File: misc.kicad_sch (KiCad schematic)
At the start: 22 parts, among them J7 Conn_ARM_JTAG_SWD_10, SW2 SW_DIP_x02, U1 MIMX8MM6DVTLZAA, Y3 24Mhz

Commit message: change USB-UART conn, add new 0402 fp, more pcb work
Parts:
- C141, C142: footprint Capacitor_SMD:C_0402_1005Metric -> qsbc:C_0402_1005Metric
- R88, R89, R90, R91, R92, R93, R94, R95, R96, R97, R98, R99: footprint Resistor_SMD:R_0402_1005Metric -> qsbc:R_0402_1005Metric
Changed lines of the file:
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@@
       (effects (font (size 1.27 1.27)) (justify left))
     )
-    (property "Footprint" "Capacitor_SMD:C_0402_1005Metric" (id 2) (at 98.7552 135.89 0)
+    (property "Footprint" "qsbc:C_0402_1005Metric" (id 2) (at 98.7552 135.89 0)
       (effects (font (size 1.27 1.27)) hide)
     )
@@
       (effects (font (size 1.27 1.27)) (justify left))
     )
-    (property "Footprint" "Resistor_SMD:R_0402_1005Metric" (id 2) (at 223.012 104.14 90)
+    (property "Footprint" "qsbc:R_0402_1005Metric" (id 2) (at 223.012 104.14 90)
       (effects (font (size 1.27 1.27)) hide)
     )
@@
       (effects (font (size 1.27 1.27)) (justify left))
     )
-    (property "Footprint" "Resistor_SMD:R_0402_1005Metric" (id 2) (at 212.852 35.56 90)
+    (property "Footprint" "qsbc:R_0402_1005Metric" (id 2) (at 212.852 35.56 90)
       (effects (font (size 1.27 1.27)) hide)
     )
@@
       (effects (font (size 1.27 1.27)) (justify left))
     )
-    (property "Footprint" "Resistor_SMD:R_0402_1005Metric" (id 2) (at 202.692 35.56 90)
+    (property "Footprint" "qsbc:R_0402_1005Metric" (id 2) (at 202.692 35.56 90)
       (effects (font (size 1.27 1.27)) hide)
     )
@@
       (effects (font (size 1.27 1.27)) (justify left))
     )
-    (property "Footprint" "Resistor_SMD:R_0402_1005Metric" (id 2) (at 94.742 58.42 90)
+    (property "Footprint" "qsbc:R_0402_1005Metric" (id 2) (at 94.742 58.42 90)
       (effects (font (size 1.27 1.27)) hide)
     )
@@
     (property "Reference" "R91" (id 0) (at 109.22 105.41 90))
     (property "Value" "510K" (id 1) (at 109.22 107.95 90))
-    (property "Footprint" "Resistor_SMD:R_0402_1005Metric" (id 2) (at 109.22 113.538 90)
+    (property "Footprint" "qsbc:R_0402_1005Metric" (id 2) (at 109.22 113.538 90)
       (effects (font (size 1.27 1.27)) hide)
     )
@@
       (effects (font (size 1.27 1.27)) (justify left))
     )
-    (property "Footprint" "Resistor_SMD:R_0402_1005Metric" (id 2) (at 233.172 104.14 90)
+    (property "Footprint" "qsbc:R_0402_1005Metric" (id 2) (at 233.172 104.14 90)
       (effects (font (size 1.27 1.27)) hide)
     )
@@
       (effects (font (size 1.27 1.27)) (justify left))
     )
-    (property "Footprint" "Resistor_SMD:R_0402_1005Metric" (id 2) (at 212.852 104.14 90)
+    (property "Footprint" "qsbc:R_0402_1005Metric" (id 2) (at 212.852 104.14 90)
       (effects (font (size 1.27 1.27)) hide)
     )
@@
       (effects (font (size 1.27 1.27)) (justify left))
     )
-    (property "Footprint" "Resistor_SMD:R_0402_1005Metric" (id 2) (at 115.062 58.42 90)
+    (property "Footprint" "qsbc:R_0402_1005Metric" (id 2) (at 115.062 58.42 90)
       (effects (font (size 1.27 1.27)) hide)
     )
@@
       (effects (font (size 1.27 1.27)) (justify left))
     )
-    (property "Footprint" "Resistor_SMD:R_0402_1005Metric" (id 2) (at 202.692 104.14 90)
+    (property "Footprint" "qsbc:R_0402_1005Metric" (id 2) (at 202.692 104.14 90)
       (effects (font (size 1.27 1.27)) hide)
     )
@@
       (effects (font (size 1.27 1.27)) (justify left))
     )
-    (property "Footprint" "Capacitor_SMD:C_0402_1005Metric" (id 2) (at 121.6152 135.89 0)
+    (property "Footprint" "qsbc:C_0402_1005Metric" (id 2) (at 121.6152 135.89 0)
       (effects (font (size 1.27 1.27)) hide)
     )
@@
       (effects (font (size 1.27 1.27)) (justify left))
     )
-    (property "Footprint" "Resistor_SMD:R_0402_1005Metric" (id 2) (at 243.332 81.28 90)
+    (property "Footprint" "qsbc:R_0402_1005Metric" (id 2) (at 243.332 81.28 90)
       (effects (font (size 1.27 1.27)) hide)
     )
@@
       (effects (font (size 1.27 1.27)) (justify left))
     )
-    (property "Footprint" "Resistor_SMD:R_0402_1005Metric" (id 2) (at 104.902 58.42 90)
+    (property "Footprint" "qsbc:R_0402_1005Metric" (id 2) (at 104.902 58.42 90)
       (effects (font (size 1.27 1.27)) hide)
     )
@@
     (property "Reference" "R90" (id 0) (at 107.95 85.09 90))
     (property "Value" "0R" (id 1) (at 107.95 87.63 90))
-    (property "Footprint" "Resistor_SMD:R_0402_1005Metric" (id 2) (at 107.95 93.218 90)
-      (effects (font (size 1.27 1.27)) hide)
-    )
+    (property "Footprint" "qsbc:R_0402_1005Metric" (id 2) (at 107.95 93.218 90)
+      (effects (font (size 1.27 1.27)) hide)
+    )

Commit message: swap usb ctrl signals for layout
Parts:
- TP22, TP23, TP24, TP25: footprint TestPoint:TestPoint_Pad_D1.0mm -> qsbc:TestPoint_Pad_D0.4mm
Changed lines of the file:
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@@
       (effects (font (size 1.27 1.27)) (justify left))
     )
-    (property "Footprint" "TestPoint:TestPoint_Pad_D1.0mm" (id 2) (at 86.36 64.77 0)
+    (property "Footprint" "qsbc:TestPoint_Pad_D0.4mm" (id 2) (at 86.36 64.77 0)
       (effects (font (size 1.27 1.27)) hide)
     )
@@
       (effects (font (size 1.27 1.27)) (justify left))
     )
-    (property "Footprint" "TestPoint:TestPoint_Pad_D1.0mm" (id 2) (at 73.66 64.77 0)
+    (property "Footprint" "qsbc:TestPoint_Pad_D0.4mm" (id 2) (at 73.66 64.77 0)
       (effects (font (size 1.27 1.27)) hide)
     )
@@
       (effects (font (size 1.27 1.27)) (justify left))
     )
-    (property "Footprint" "TestPoint:TestPoint_Pad_D1.0mm" (id 2) (at 48.26 64.77 0)
+    (property "Footprint" "qsbc:TestPoint_Pad_D0.4mm" (id 2) (at 48.26 64.77 0)
       (effects (font (size 1.27 1.27)) hide)
     )
@@
       (effects (font (size 1.27 1.27)) (justify left))
     )
-    (property "Footprint" "TestPoint:TestPoint_Pad_D1.0mm" (id 2) (at 60.96 64.77 0)
-      (effects (font (size 1.27 1.27)) hide)
-    )
+    (property "Footprint" "qsbc:TestPoint_Pad_D0.4mm" (id 2) (at 60.96 64.77 0)
+      (effects (font (size 1.27 1.27)) hide)
+    )

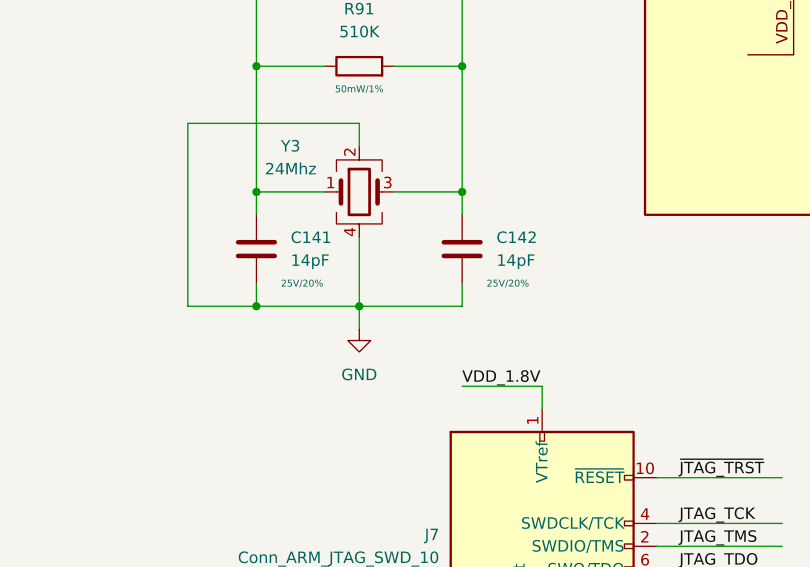
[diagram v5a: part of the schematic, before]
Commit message: bom work, change uart level shifter and m.2 socket
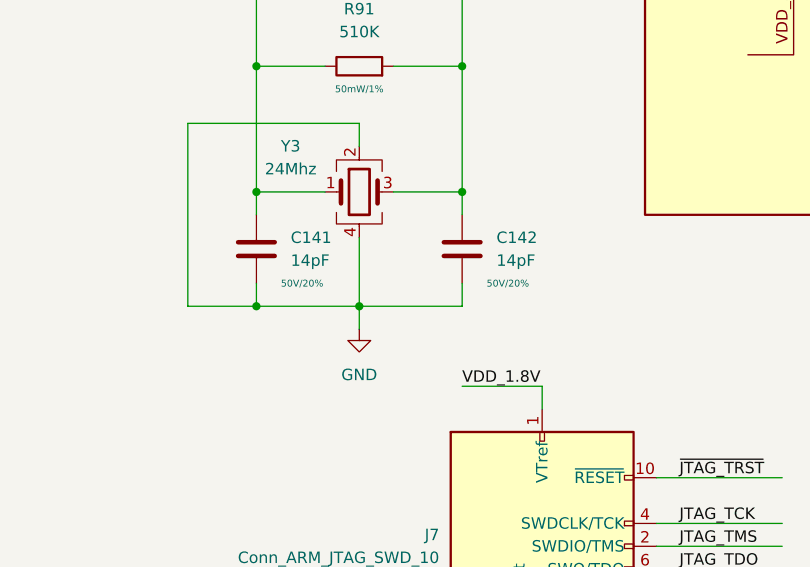
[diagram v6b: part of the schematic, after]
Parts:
- C141, C142: MPN (none) -> 04025U140FAT2A; Rating 25V/20% -> 50V/20%
- J7: MPN (none) -> FTSH-105-01-F-D-007-K
- R88, R89, R92, R94, R98: MPN (none) -> RC0402FR-07100KL
- R90: MPN (none) -> RC0402FR-070RL
- R91: MPN (none) -> RC0402FR-07510KL
- R93, R95, R96, R97, R99: MPN (none) -> RC0402FR-0710KL
- SW2: MPN (none) -> DHN-02-V-T/R
- U1: MPN (none) -> MIMX8MM6DVTLZAA
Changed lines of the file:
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@@
       (effects (font (size 1.27 1.27)) hide)
     )
-    (property "Rating" "25V/20%" (id 4) (at 102.87 135.89 0)
-      (effects (font (size 0.762 0.762)))
+    (property "Rating" "50V/20%" (id 4) (at 102.87 135.89 0)
+      (effects (font (size 0.762 0.762)))
+    )
+    (property "MPN" "04025U140FAT2A" (id 5) (at 97.79 132.08 0)
+      (effects (font (size 1.27 1.27)) hide)
     )
     (pin "1")
@@
     (property "Rating" "50mW/1%" (id 4) (at 229.87 107.95 0)
       (effects (font (size 0.762 0.762)))
+    )
+    (property "MPN" "RC0402FR-0710KL" (id 5) (at 224.79 104.14 0)
+      (effects (font (size 1.27 1.27)) hide)
     )
     (pin "1")
@@
     (property "Datasheet" "https://www.nxp.com/docs/en/data-sheet/IMX8MMCEC.pdf" (id 3) (at 162.56 265.43 0)
       (effects (font (size 1.27 1.27)) (justify left bottom) hide)
+    )
+    (property "MPN" "MIMX8MM6DVTLZAA" (id 4) (at 161.29 71.12 0)
+      (effects (font (size 1.27 1.27)) hide)
     )
     (pin "A24")
@@
       (effects (font (size 0.762 0.762)))
     )
+    (property "MPN" "RC0402FR-0710KL" (id 5) (at 214.63 35.56 0)
+      (effects (font (size 1.27 1.27)) hide)
+    )
     (pin "1")
     (pin "2")
@@
       (effects (font (size 0.762 0.762)))
     )
+    (property "MPN" "RC0402FR-0710KL" (id 5) (at 204.47 35.56 0)
+      (effects (font (size 1.27 1.27)) hide)
+    )
     (pin "1")
     (pin "2")
@@
     (property "Rating" "50mW/1%" (id 4) (at 101.6 62.23 0)
       (effects (font (size 0.762 0.762)))
+    )
+    (property "MPN" "RC0402FR-07100KL" (id 5) (at 96.52 58.42 0)
+      (effects (font (size 1.27 1.27)) hide)
     )
     (pin "1")
@@
       (effects (font (size 0.762 0.762)))
     )
+    (property "MPN" "RC0402FR-07510KL" (id 5) (at 109.22 111.76 0)
+      (effects (font (size 1.27 1.27)) hide)
+    )
     (pin "1")
     (pin "2")
@@
       (effects (font (size 0.762 0.762)))
     )
+    (property "MPN" "RC0402FR-07100KL" (id 5) (at 234.95 104.14 0)
+      (effects (font (size 1.27 1.27)) hide)
+    )
     (pin "1")
     (pin "2")
@@
       (effects (font (size 0.762 0.762)))
     )
+    (property "MPN" "RC0402FR-0710KL" (id 5) (at 214.63 104.14 0)
+      (effects (font (size 1.27 1.27)) hide)
+    )
     (pin "1")
     (pin "2")
@@
     (property "Rating" "50mW/1%" (id 4) (at 121.92 62.23 0)
       (effects (font (size 0.762 0.762)))
+    )
+    (property "MPN" "RC0402FR-07100KL" (id 5) (at 116.84 58.42 0)
+      (effects (font (size 1.27 1.27)) hide)
     )
     (pin "1")
@@
       (effects (font (size 0.762 0.762)))
     )
+    (property "MPN" "RC0402FR-07100KL" (id 5) (at 204.47 104.14 0)
+      (effects (font (size 1.27 1.27)) hide)
+    )
     (pin "1")
     (pin "2")
@@
       (effects (font (size 1.27 1.27)) hide)
     )
-    (property "Rating" "25V/20%" (id 4) (at 125.73 135.89 0)
-      (effects (font (size 0.762 0.762)))
+    (property "Rating" "50V/20%" (id 4) (at 125.73 135.89 0)
+      (effects (font (size 0.762 0.762)))
+    )
+    (property "MPN" "04025U140FAT2A" (id 5) (at 120.65 132.08 0)
+      (effects (font (size 1.27 1.27)) hide)
     )
     (pin "1")
@@
       (effects (font (size 0.762 0.762)))
     )
+    (property "MPN" "RC0402FR-0710KL" (id 5) (at 245.11 81.28 0)
+      (effects (font (size 1.27 1.27)) hide)
+    )
     (pin "1")
     (pin "2")
@@
     (property "Rating" "50mW/1%" (id 4) (at 111.76 62.23 0)
       (effects (font (size 0.762 0.762)))
+    )
+    (property "MPN" "RC0402FR-07100KL" (id 5) (at 106.68 58.42 0)
+      (effects (font (size 1.27 1.27)) hide)
     )
     (pin "1")
@@
     )
     (property "Datasheet" "~" (id 3) (at 207.01 52.07 0)
+      (effects (font (size 1.27 1.27)) hide)
+    )
+    (property "MPN" "DHN-02-V-T/R" (id 4) (at 207.01 52.07 0)
       (effects (font (size 1.27 1.27)) hide)
     )
@@
       (effects (font (size 1.27 1.27)) hide)
     )
+    (property "MPN" "RC0402FR-070RL" (id 4) (at 107.95 91.44 0)
+      (effects (font (size 1.27 1.27)) hide)
+    )
     (pin "1")
     (pin "2")
@@
       (effects (font (size 1.27 1.27)) hide)
     )
+    (property "MPN" "FTSH-105-01-F-D-007-K" (id 4) (at 129.54 165.1 0)
+      (effects (font (size 1.27 1.27)) hide)
+    )

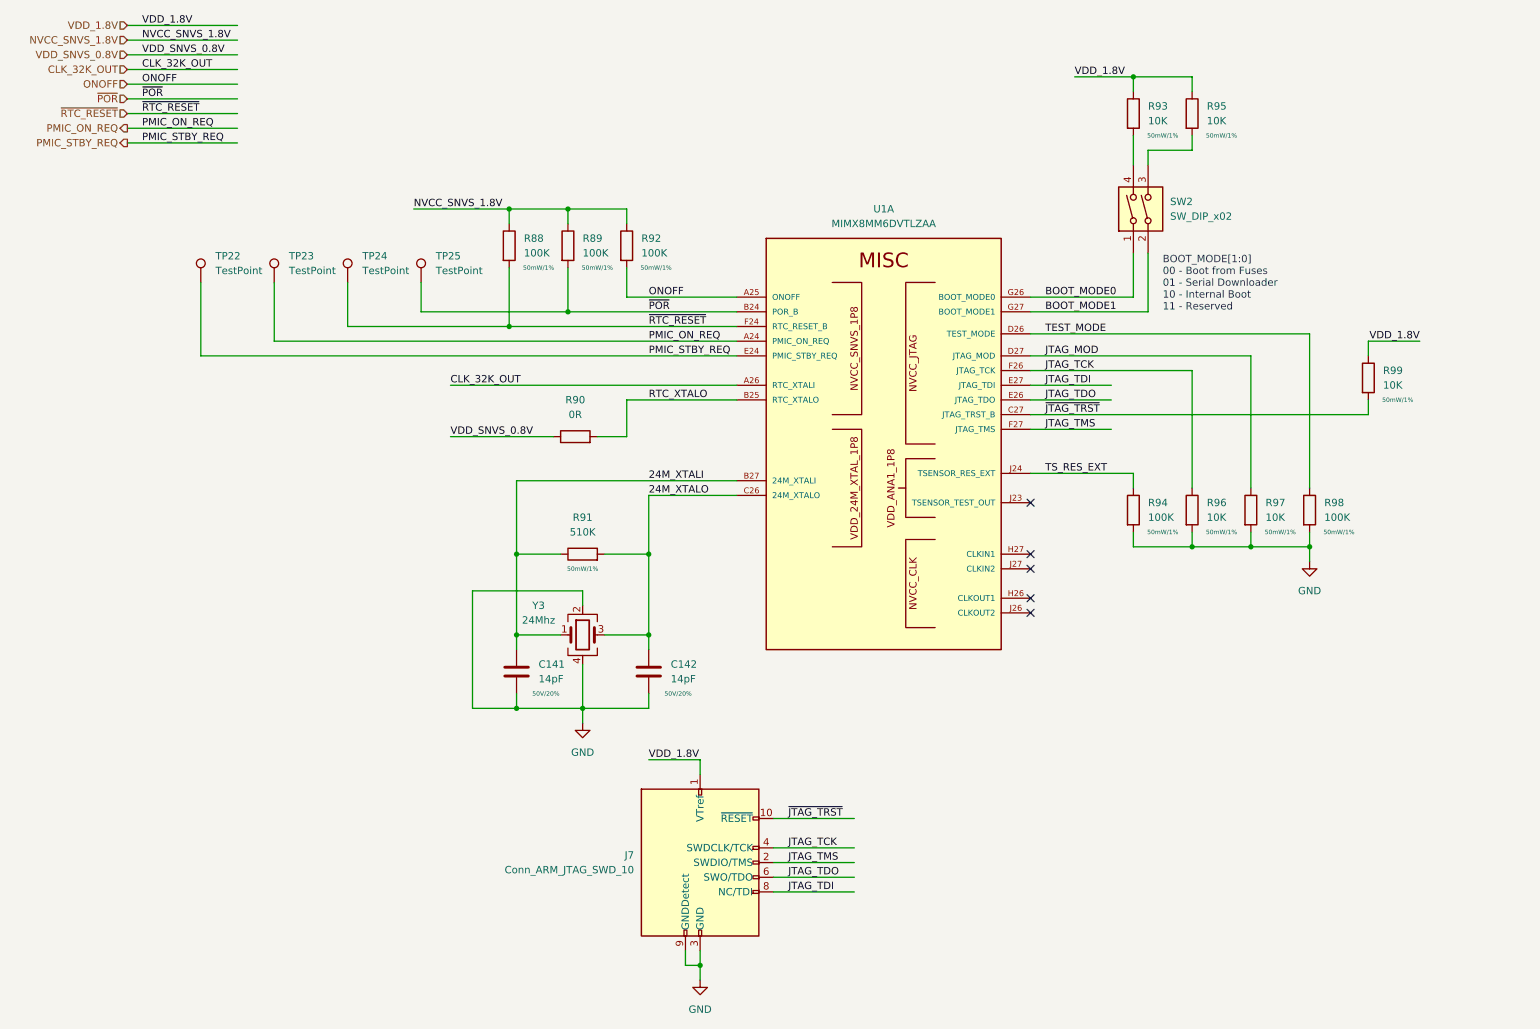
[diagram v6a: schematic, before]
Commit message: ddr length matching work, misc cleanup
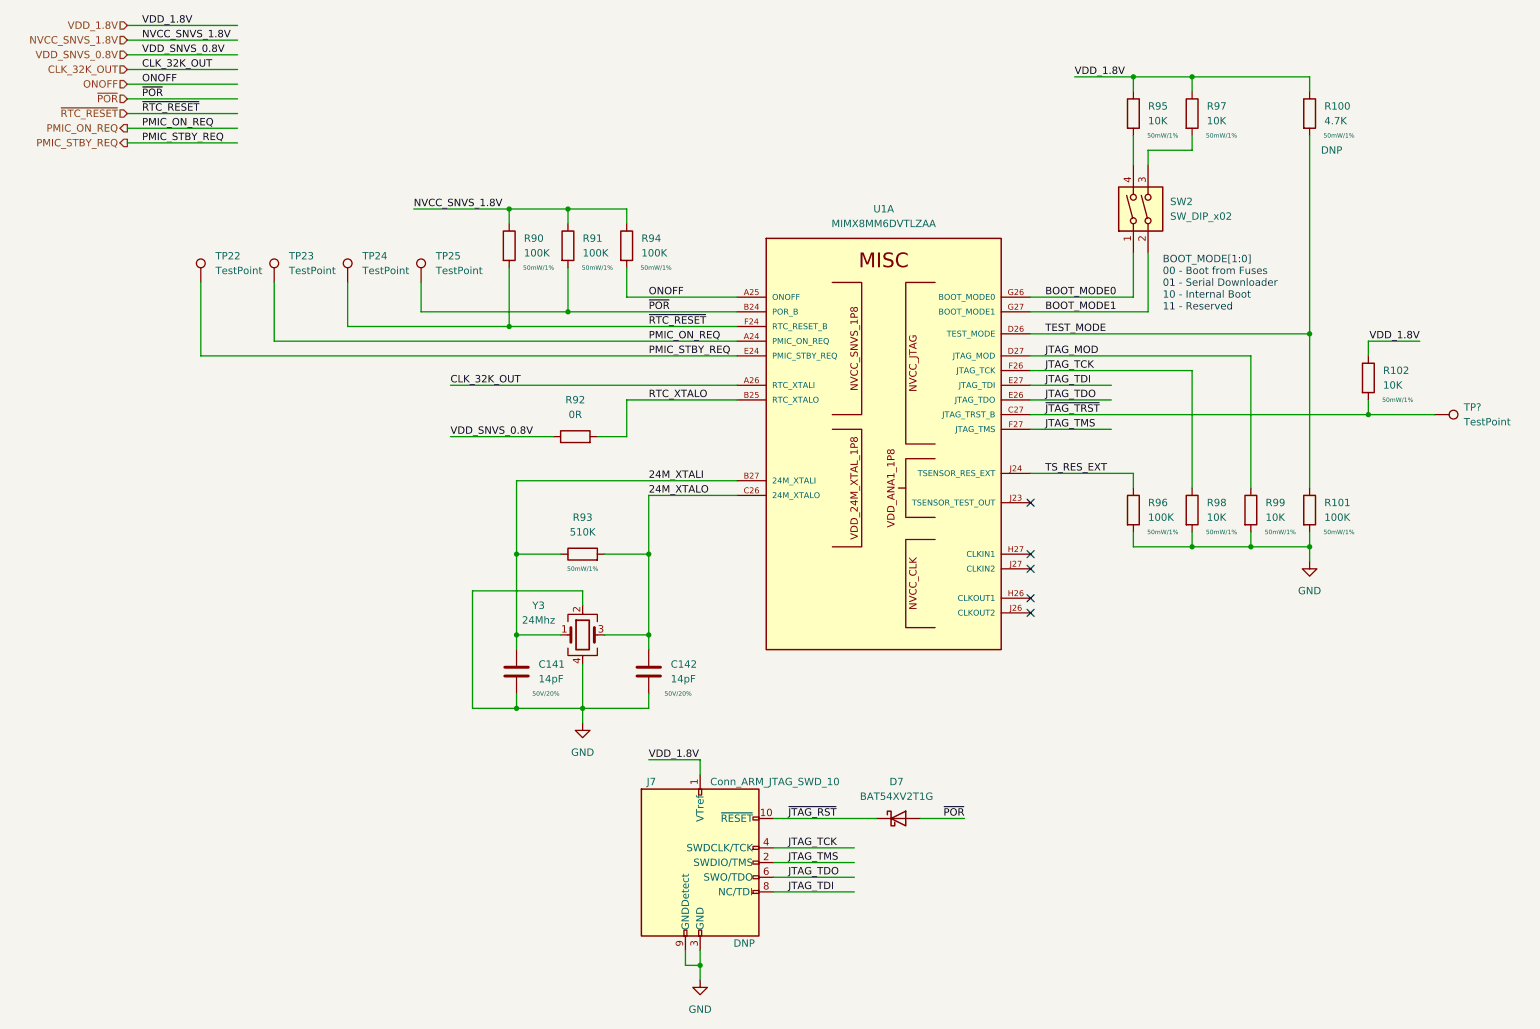
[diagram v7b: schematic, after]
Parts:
- added D7: BAT54XV2T1G, Diode_SMD:D_SOD-523, symbol Device:D_Schottky
- added R100: 4.7K, qsbc:R_0402_1005Metric, symbol Device:R
- added TP?: TestPoint, qsbc:TestPoint_Pad_D0.4mm, symbol Connector:TestPoint
- J7: DNP (none) -> DNP
- renumbered R98 to R101, R99 to R102, R88 to R90, R89 to R91, R90 to R92, R91 to R93, R92 to R94, R93 to R95, R94 to R96, R95 to R97, R96 to R98, R97 to R99
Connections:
- net TEST_MODE: now also R100.2
- net VDD_1.8V: now also R100.1
- net ~{JTAG_TRST}: now also TP?.1; no longer J7.10 (~{RESET})
- net ~{POR}: now also D7.2 (A)
- new net ~{JTAG_RST}: D7.1 (K), J7.10 (~{RESET})
